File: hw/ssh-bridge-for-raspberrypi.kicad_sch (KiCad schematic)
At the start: 38 parts, among them J101 USB4105-GF-A, J102 USB4105-GF-A, J103 PinHeader Conn_01x08, J104 Conn_02x05_Odd_Even, J105 USB_A, J106 Conn_01x03, SW304 1, U101 ST7789V_TFT_DISPLAY_8P, U102 TLP3555A, U103 AZ1117-CH3.3TRG1, U201 ESP32-S3-WROOM-1-N16R8

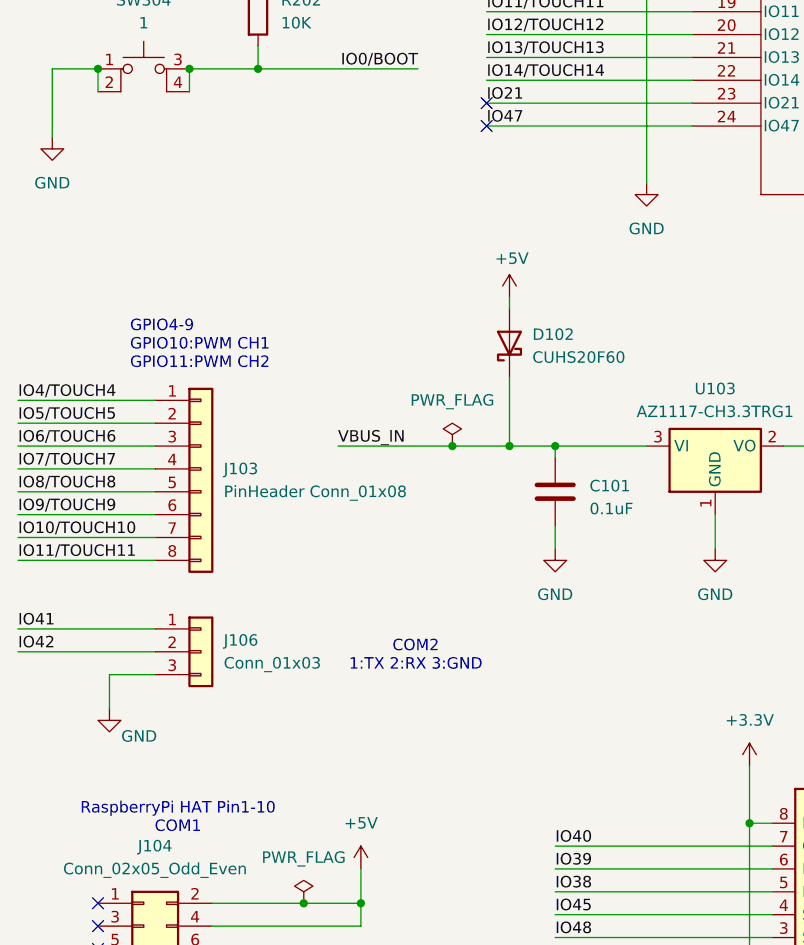
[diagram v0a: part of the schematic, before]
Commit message: ssh-serrial-bridge for raspberrypi
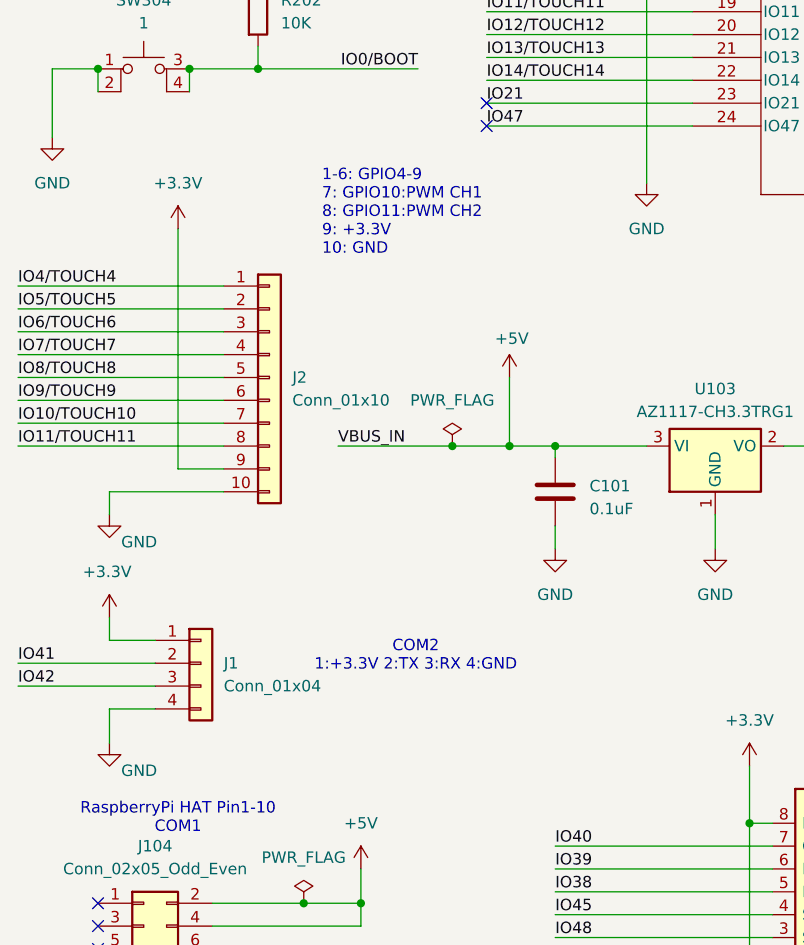
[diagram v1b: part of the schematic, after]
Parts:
- removed D102: CUHS20F60, Diode_SMD:D_PowerDI-123, symbol tbctl:SK36A-LTP
- removed J103: PinHeader Conn_01x08, Connector_PinHeader_2.54mm:PinHeader_1x08_P2.54mm_Vertical, symbol tbctl:PinHeader Conn_01x08
- removed J106: Conn_01x03, Connector_PinHeader_2.54mm:PinHeader_1x03_P2.54mm_Vertical, symbol Connector_Generic:Conn_01x03
- added J1: Conn_01x04, Connector_PinHeader_2.54mm:PinHeader_1x04_P2.54mm_Vertical, symbol Connector_Generic:Conn_01x04
- added J2: Conn_01x10, Connector_PinHeader_2.54mm:PinHeader_1x10_P2.54mm_Vertical, symbol Connector_Generic:Conn_01x10
- C203: digikey 311-3494-1-ND -> 311-1355-1-ND
- D101: digikey SK36A-LTPMSCT-ND -> 264-CUHS20F60H3FCT-ND
- D103: digikey 3147-B1931NB--20C007614U1930CT-ND -> 3147-B1931URO-20D000114U1930CT-ND
- J104: digikey (none) -> 732-2672-ND
- J105: digikey (none) -> ED2989-ND
- R101: digikey 311-4.70KHRCT-ND -> 13-RC0603FR-13150RLCT-ND
- R104, R109: digikey 311-5.10KHRCT-ND -> 311-75.0KHRCT-ND
- R105: digikey 311-3.09KHRCT-ND -> 13-RC0603JR-13330RLCT-ND
- R108: digikey 311-3.09KHRCT-ND -> 311-1.00KHRCT-ND
- R110, R111: digikey 311-5.10KHRCT-ND -> 311-51.0KHRCT-ND
- R201, R202: digikey 13-RC0603JR-1010KLCT-ND -> 311-10.0KHRCT-ND
- SW304: digikey (none) -> P12298SCT-ND
- TP103: digikey (none) -> -
- U102: digikey (none) -> TLP3555A(F-ND
- U103: digikey 497-1242-1-ND -> AZ1117CH-3.3TRG1DICT-ND
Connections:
- net VBUS_IN is gone; now on net +5V: C101.1, D101.1 (K), J101.A4 (VBUS), J101.A9 (VBUS), J101.B4 (VBUS), J101.B9 (VBUS), R204.1, U102.4, U103.3 (VI)
- net +3.3V: now also J1.1 (Pin_1), J2.9 (Pin_9)
- net GND: now also J1.4 (Pin_4), J2.10 (Pin_10)
- net IO10/TOUCH10: now also J2.7 (Pin_7)
- net IO11/TOUCH11: now also J2.8 (Pin_8)
- net IO41: now also J1.2 (Pin_2)
- net IO42: now also J1.3 (Pin_3)
- net IO4/TOUCH4: now also J2.1 (Pin_1)
- net IO5/TOUCH5: now also J2.2 (Pin_2)
- net IO6/TOUCH6: now also J2.3 (Pin_3)
- net IO7/TOUCH7: now also J2.4 (Pin_4)
- net IO8/TOUCH8: now also J2.5 (Pin_5)
- net IO9/TOUCH9: now also J2.6 (Pin_6)
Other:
- note added: "1-6: GPIO4-9 7: GPIO10:PWM CH1 8: GPIO11:PWM CH2 9: +3.3V 10: GND"
- note added: "COM2 1:+3.3V 2:TX 3:RX 4:GND"
- note removed: "COM2 1:TX 2:RX 3:GND"
- note removed: "GPIO4-9 GPIO10:PWM CH1 GPIO11:PWM CH2"
